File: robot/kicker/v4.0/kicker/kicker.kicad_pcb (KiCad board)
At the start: 6 copper layers, 172.6 x 120 mm, 181 parts, among them J1 BM08B-GHS-TBT, J10 SM08B-GHS-TB, J2 BM04B-PASS-1-TFT, J3 XT30-F, J4 Conn_ARM_JTAG_SWD_10, J5 2165711002, J6 2165711002, J7 SM12B-ZESS-TB, J8 SM08B-GHS-TB, J9 SM08B-GHS-TB, Q1 BSS138K, Q2 BSS138K, Q3 IXGA48N60A3, Q4 IXGA48N60A3, Q5 BSC0402NSATMA1, SW1 BTN0, SW2 SW_DIP_x04, SW3 RST, U1 TLV70030_SOT353, U2 TPS7B86, U3 STM32G474VETx, U4 SK9822, U5 AT25DF041x-UxN-x, U6 SK9822, U7 IX4427, U8 LT3757EMSE, Y1 Q13FC13500005, Y2 TAXM8M4RDBCCT2T

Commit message: Set preferred bank capacitor PN
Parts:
- C25, C26: value 1500uF 200V -> ESMQ201VSN152MR35S
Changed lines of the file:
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@@
 			)
 		)
-		(property "Value" "1500uF 200V"
+		(property "Value" "ESMQ201VSN152MR35S"
 			(at 5 -16.25 90)
 			(layer "B.Fab")
@@
 			)
 		)
+		(property "Value2" "1500uF 200V"
+			(at 0 0 -90)
+			(unlocked yes)
+			(layer "B.Fab")
+			(hide yes)
+			(effects
+				(font
+					(size 1 1)
+					(thickness 0.15)
+				)
+				(justify mirror)
+			)
+		)
 		(property ki_fp_filters "CP_*")
 		(sheetname "hv_kicker")
@@
 			)
 		)
-		(property "Value" "1500uF 200V"
+		(property "Value" "ESMQ201VSN152MR35S"
 			(at 5 -16.25 90)
 			(layer "B.Fab")
@@
 					(thickness 0.15)
 				)
+				(justify mirror)
+			)
+		)
+		(property "Value2" "1500uF 200V"
+			(at 0 0 -90)
+			(unlocked yes)
+			(layer "B.Fab")
+			(hide yes)
+			(effects
+				(font
+					(size 1 1)
+					(thickness 0.15)
+				)

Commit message: Update potentiometer values
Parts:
- RV1: value ACFG1 -> 3269P-1-103GLF
- RV2: value ACFG2 -> 3269P-1-103GLF
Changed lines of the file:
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@@
 		(tags "resistor")
 		(property "Reference" "R11"
-			(at -2.5 0 360)
+			(at -2.5 0 0)
 			(layer "F.SilkS")
 			(effects
@@
 		)
 		(property "Value" "10k"
-			(at 0 1.17 360)
+			(at 0 1.17 0)
 			(layer "F.Fab")
 			(effects
@@
 		)
 		(fp_text user "${REFERENCE}"
-			(at 0 0 360)
+			(at 0 0 0)
 			(layer "F.Fab")
 			(effects
@@
 		(tags "resistor")
 		(property "Reference" "R22"
-			(at 0 -1.25 360)
+			(at 0 -1.25 0)
 			(layer "F.SilkS")
 			(effects
@@
 		)
 		(property "Value" "10k"
-			(at 0 1.17 360)
+			(at 0 1.17 0)
 			(layer "F.Fab")
 			(effects
@@
 		)
 		(fp_text user "${REFERENCE}"
-			(at 0 0 360)
+			(at 0 0 0)
 			(layer "F.Fab")
 			(effects
@@
 		(tags "resistor")
 		(property "Reference" "R50"
-			(at 0 -1.65 360)
+			(at 0 -1.65 0)
 			(layer "F.SilkS")
 			(effects
@@
 		)
 		(property "Value" "1.47M"
-			(at 0 1.65 360)
+			(at 0 1.65 0)
 			(layer "F.Fab")
 			(effects
@@
 		)
 		(fp_text user "${REFERENCE}"
-			(at 0 0 360)
+			(at 0 0 0)
 			(layer "F.Fab")
 			(effects
@@
 		(tags "capacitor")
 		(property "Reference" "C5"
-			(at 0 1.25 360)
+			(at 0 1.25 0)
 			(layer "F.SilkS")
 			(effects
@@
 		)
 		(property "Value" "10u 50V"
-			(at 0 1.16 360)
+			(at 0 1.16 0)
 			(layer "F.Fab")
 			(effects
@@
 		)
 		(fp_text user "${REFERENCE}"
-			(at 0 0 360)
+			(at 0 0 0)
 			(layer "F.Fab")
 			(effects
@@
 			)
 		)
-		(property "Value" "ACFG1"
+		(property "Value" "3269P-1-103GLF"
 			(at 0 4.425001 135)
 			(layer "F.Fab")
@@
 			)
 		)
+		(property "Value2" "10k"
+			(at 0 0 135)
+			(unlocked yes)
+			(layer "F.Fab")
+			(hide yes)
+			(effects
+				(font
+					(size 1 1)
+					(thickness 0.15)
+				)
+			)
+		)
 		(property ki_fp_filters "Potentiometer*")
 		(sheetname "digital")
@@
 		(at 248 173 90)
 		(property "Reference" "SW2"
-			(at -4.75 0 360)
+			(at -4.75 0 0)
 			(layer "F.SilkS")
 			(effects
@@
 		(tags "resistor")
 		(property "Reference" "R10"
-			(at 0 1.5 360)
+			(at 0 1.5 0)
 			(layer "F.SilkS")
 			(effects
@@
 		)
 		(property "Value" "10k"
-			(at 0 1.17 360)
+			(at 0 1.17 0)
 			(layer "F.Fab")
 			(effects
@@
 		)
 		(fp_text user "${REFERENCE}"
-			(at 0 0 360)
+			(at 0 0 0)
 			(layer "F.Fab")
 			(effects
@@
 		(tags "resistor")
 		(property "Reference" "R20"
-			(at 2.5 0.25 360)
+			(at 2.5 0.25 0)
 			(layer "F.SilkS")
 			(effects
@@
 		)
 		(property "Value" "330"
-			(at 0 1.17 360)
+			(at 0 1.17 0)
 			(layer "F.Fab")
 			(effects
@@
 		)
 		(fp_text user "${REFERENCE}"
-			(at 0 0 360)
+			(at 0 0 0)
 			(layer "F.Fab")
 			(effects
@@
 		(tags "capacitor")
 		(property "Reference" "C6"
-			(at -2.5 0.25 360)
+			(at -2.5 0.25 0)
 			(layer "F.SilkS")
 			(effects
@@
 		)
 		(property "Value" "100n 50V"
-			(at 0 1.16 360)
+			(at 0 1.16 0)
 			(layer "F.Fab")
 			(effects
@@
 		)
 		(fp_text user "${REFERENCE}"
-			(at 0 0 360)
+			(at 0 0 0)
 			(layer "F.Fab")
 			(effects
@@
 		(tags "resistor")
 		(property "Reference" "R44"
-			(at -2.5 -0.25 360)
+			(at -2.5 -0.25 0)
 			(layer "F.SilkS")
 			(effects
@@
 		)
 		(property "Value" "10k"
-			(at 0 1.17 360)
+			(at 0 1.17 0)
 			(layer "F.Fab")
 			(effects
@@
 		)
 		(fp_text user "${REFERENCE}"
-			(at 0 0 360)
+			(at 0 0 0)
 			(layer "F.Fab")
 			(effects
@@
 		(tags "Diode SMC (DO-214AB)")
 		(property "Reference" "D12"
-			(at 0 4.500001 360)
+			(at 0 4.500001 0)
 			(layer "F.SilkS")
 			(effects
@@
 		)
 		(property "Value" "MURS460"
-			(at 0 4.199999 360)
+			(at 0 4.199999 0)
 			(layer "F.Fab")
 			(effects
@@
 		)
 		(fp_text user "${REFERENCE}"
-			(at 0 -1.9 360)
+			(at 0 -1.9 0)
 			(layer "F.Fab")
 			(effects
@@
 		(tags "resistor")
 		(property "Reference" "R38"
-			(at -2.5 -0.5 360)
+			(at -2.5 -0.5 0)
 			(layer "F.SilkS")
 			(effects
@@
 		)
 		(property "Value" "23.2k"
-			(at 0 1.17 360)
+			(at 0 1.17 0)
 			(layer "F.Fab")
 			(effects
@@
 		)
 		(fp_text user "${REFERENCE}"
-			(at 0 0 360)
+			(at 0 0 0)
 			(layer "F.Fab")
 			(effects
@@
 		(tags "resistor")
 		(property "Reference" "R49"
-			(at 0 -1.65 360)
+			(at 0 -1.65 0)
 			(layer "F.SilkS")
 			(effects
@@
 		)
 		(property "Value" "1.47M"
-			(at 0 1.65 360)
+			(at 0 1.65 0)
 			(layer "F.Fab")
 			(effects
@@
 		)
 		(fp_text user "${REFERENCE}"
-			(at 0 0 360)
+			(at 0 0 0)
 			(layer "F.Fab")
 			(effects
@@
 		(tags "resistor")
 		(property "Reference" "R57"
-			(at 2.5 0 360)
+			(at 2.5 0 0)
 			(layer "F.SilkS")
 			(effects
@@
 		)
 		(property "Value" "10"
-			(at 0 1.17 360)
+			(at 0 1.17 0)
 			(layer "F.Fab")
 			(effects
@@
 		)
 		(fp_text user "${REFERENCE}"
-			(at 0 0 360)
+			(at 0 0 0)
 			(layer "F.Fab")
 			(effects
@@
 		(tags "resistor")
 		(property "Reference" "R31"
-			(at -2.5 0 360)
+			(at -2.5 0 0)
 			(layer "F.SilkS")
 			(effects
@@
 		)
 		(property "Value" "10k"
-			(at 0 1.17 360)
+			(at 0 1.17 0)
 			(layer "F.Fab")
 			(effects
@@
 		)
 		(fp_text user "${REFERENCE}"
-			(at 0 0 360)
+			(at 0 0 0)
 			(layer "F.Fab")
 			(effects
@@
 		(tags "resistor")
 		(property "Reference" "R1"
-			(at -0.2 -2.3 360)
+			(at -0.2 -2.3 0)
 			(layer "F.SilkS")
 			(effects
@@
 		)
 		(property "Value" "330"
-			(at 0 1.17 360)
+			(at 0 1.17 0)
 			(layer "F.Fab")
 			(effects
@@
 		)
 		(fp_text user "${REFERENCE}"
-			(at 0 0 360)
+			(at 0 0 0)
 			(layer "F.Fab")
 			(effects
@@
 			)
 		)
-		(property "Value" "ACFG2"
+		(property "Value" "3269P-1-103GLF"
 			(at 0 4.425001 135)
 			(layer "F.Fab")
@@
 			)
 		)
+		(property "Value2" "10k"
+			(at 0 0 135)
+			(unlocked yes)
+			(layer "F.Fab")
+			(hide yes)
+			(effects
+				(font
+					(size 1 1)
+					(thickness 0.15)
+				)
+			)
+		)
 		(property ki_fp_filters "Potentiometer*")
 		(sheetname "digital")
@@
 		(tags "resistor")
 		(property "Reference" "R35"
-			(at -2.5 0.25 360)
+			(at -2.5 0.25 0)
 			(layer "F.SilkS")
 			(effects
@@
 		)
 		(property "Value" "10k"
-			(at 0 1.17 360)
+			(at 0 1.17 0)
 			(layer "F.Fab")
 			(effects
@@
 		)
 		(fp_text user "${REFERENCE}"
-			(at 0 0 360)
+			(at 0 0 0)
 			(layer "F.Fab")
 			(effects
@@
 		(at 180 144)
 		(property "Reference" "F3"
-			(at 0 4.500001 360)
+			(at 0 4.500001 0)
 			(layer "B.SilkS")
 			(effects
@@
 		)
 		(property "Value" "10A"
-			(at 0 -4.500001 360)
+			(at 0 -4.500001 0)
 			(layer "B.Fab")
 			(effects
@@
 		)
 		(property "Footprint" "AT-Fuses:3557-2"
-			(at 0 0 360)
+			(at 0 0 0)
 			(layer "B.Fab")
 			(hide yes)
@@
 		)
 		(property "Datasheet" ""
-			(at 0 0 360)
+			(at 0 0 0)
 			(layer "B.Fab")
 			(hide yes)
@@
 		)
 		(property "Description" "Fuse"
-			(at 0 0 360)
+			(at 0 0 0)
 			(layer "B.Fab")
 			(hide yes)
@@
 		)
 		(fp_text user "${REFERENCE}"
-			(at 0 0 360)
+			(at 0 0 0)
 			(layer "B.Fab")
 			(effects
@@
 		)
 		(property "Footprint" "AT-Connectors:2165711002"
-			(at 0 0 360)
+			(at 0 0 0)
 			(layer "B.Fab")
 			(hide yes)
@@
 		)
 		(property "Datasheet" ""
-			(at 0 0 360)
+			(at 0 0 0)
 			(layer "B.Fab")
 			(hide yes)
@@
 		)
 		(property "Description" "Generic connector, single row, 01x02, script generated (kicad-library-utils/schlib/autogen/connector/)"
-			(at 0 0 360)
+			(at 0 0 0)
 			(layer "B.Fab")
 			(hide yes)
@@
 		)
 		(property "Footprint" "AT-Connectors:2165711002"
-			(at 0 0 360)
+			(at 0 0 0)
 			(layer "B.Fab")
 			(hide yes)
@@
 		)
 		(property "Datasheet" ""
-			(at 0 0 360)
+			(at 0 0 0)
 			(layer "B.Fab")
 			(hide yes)
@@
 		)
 		(property "Description" "Generic connector, single row, 01x02, script generated (kicad-library-utils/schlib/autogen/connector/)"
-			(at 0 0 360)
+			(at 0 0 0)
 			(layer "B.Fab")
 			(hide yes)

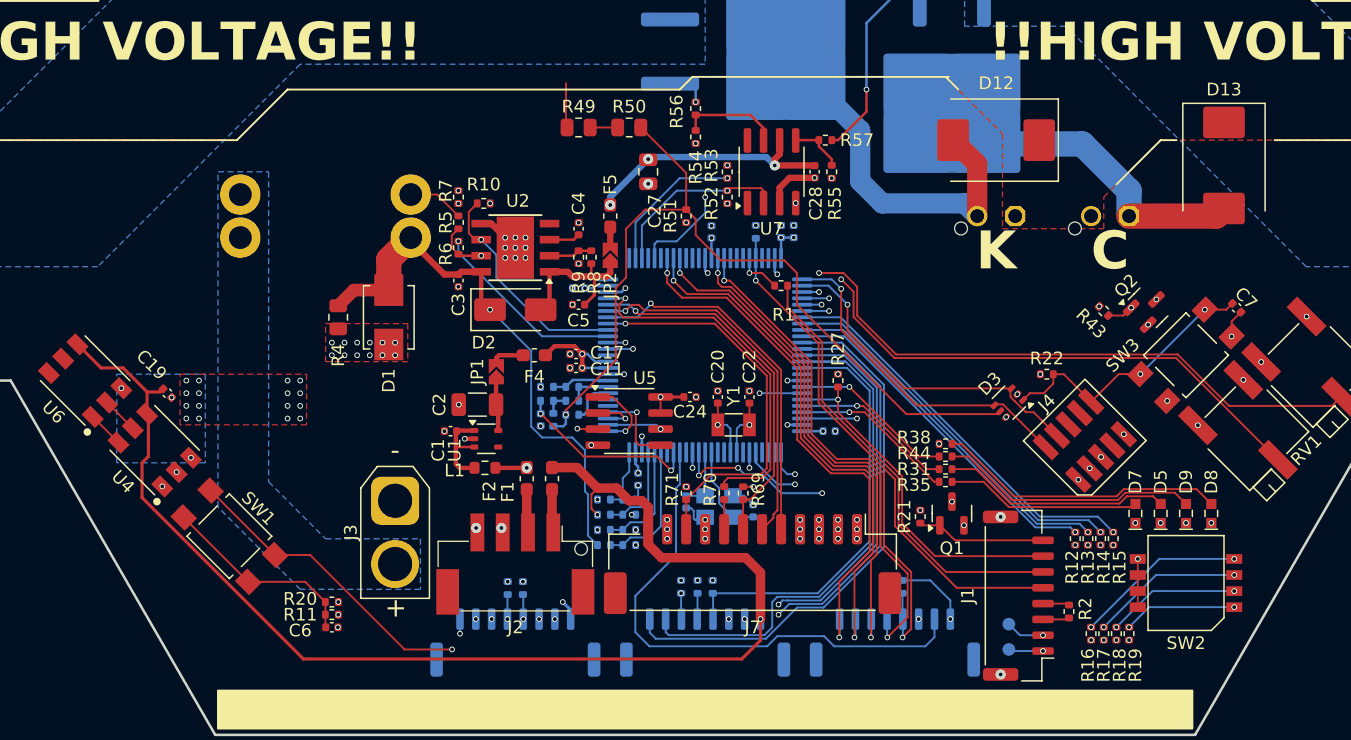
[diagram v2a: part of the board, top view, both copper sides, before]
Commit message: Update silkscreen & current sense resistor values
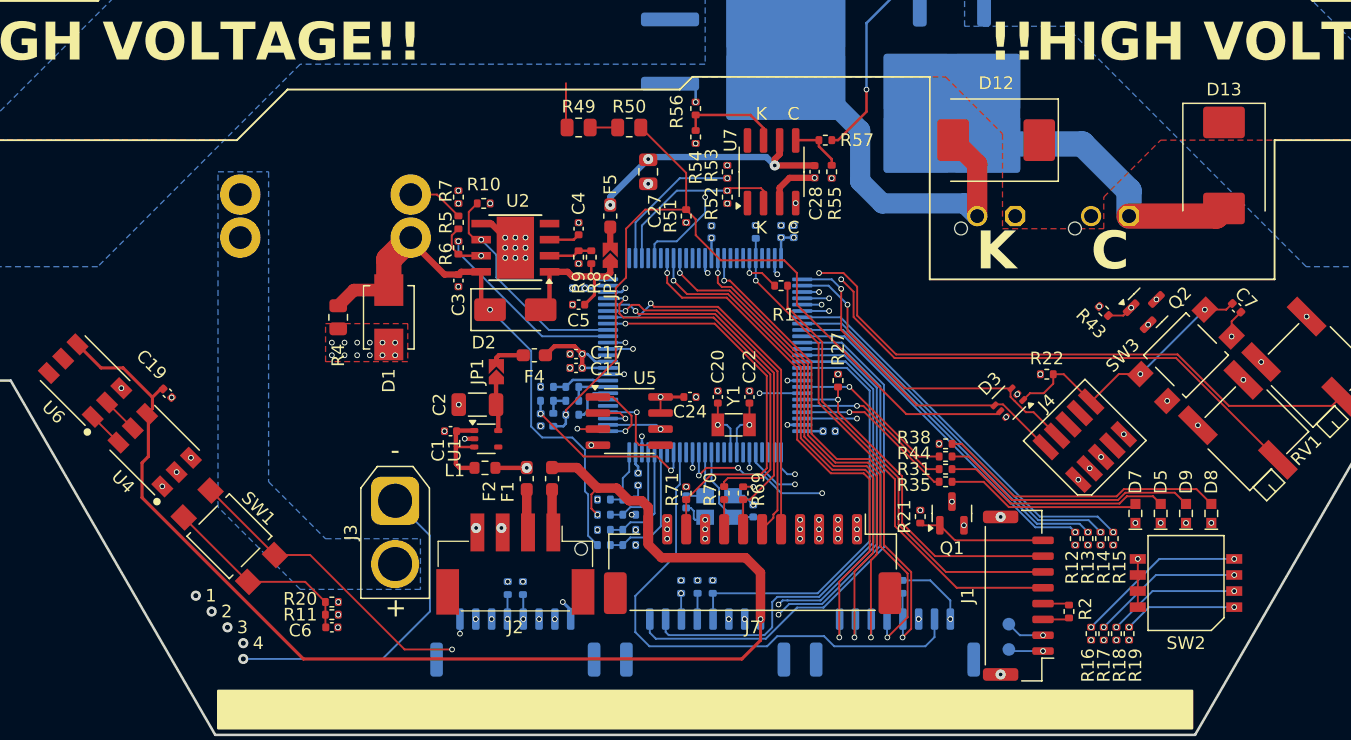
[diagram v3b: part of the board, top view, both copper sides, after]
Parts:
- R64, R65: value 4m -> PE1206FRM470R008L
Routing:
- net GND: track 84.9 -> 126.7 mm, vias 213 -> 202
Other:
- board text added: "1"
- board text added: "2"
- board text added: "3"
- board text added: "4"

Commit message: layout after connector fix done
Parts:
- removed J10: SM08B-GHS-TB, Connector_JST:JST_GH_SM08B-GHS-TB_1x08-1MP_P1.25mm_Horizontal
- added J11: JST-SM10B-GHS, Connector_JST:JST_GH_SM10B-GHS-TB_1x10-1MP_P1.25mm_Horizontal, F.Cu at (234.7, 172.6)
- added R79: 330, Resistor_SMD:R_0402_1005Metric, F.Cu at (207.5, 165.9)
- added R80: 100k, Resistor_SMD:R_0402_1005Metric, B.Cu at (214.9, 171.7)
- added R81: 100k, Resistor_SMD:R_0402_1005Metric, B.Cu at (216.0, 171.7)
- added R82: 100k, Resistor_SMD:R_0402_1005Metric, B.Cu at (234.4, 178.3)
- added R83: 100k, Resistor_SMD:R_0402_1005Metric, B.Cu at (234.4, 172.0)
- added R84: 100k, Resistor_SMD:R_0402_1005Metric, B.Cu at (234.4, 173.2)
- added R85: 330, Resistor_SMD:R_0402_1005Metric, F.Cu at (204.4, 177.9)
- added R86: 100k, Resistor_SMD:R_0402_1005Metric, F.Cu at (209.4, 177.9)
- added R87: 100k, Resistor_SMD:R_0402_1005Metric, F.Cu at (210.7, 177.9)
- J1: value BM08B-GHS-TBT -> JST-SM10B-GHS; footprint Connector_JST:JST_GH_BM08B-GHS-TBT_1x08-1MP_P1.25mm_Vertical -> Connector_JST:JST_GH_SM10B-GHS-TB_1x10-1MP_P1.25mm_Horizontal; moved to B.Cu
- R2, R69, R71: moved to B.Cu
- R76, R77, R78: moved to F.Cu
- moved J1 25.0 mm to (210.0, 177.7), turned to 180 degrees
- moved TP1 11.7 mm to (234.1, 166.6), turned to -135 degrees
- moved TP2 7.65 mm to (234.1, 168.6), turned to -135 degrees
- moved R77 5.90 mm to (206.9, 177.9), turned to 90 degrees
- moved R76 5.24 mm to (205.6, 177.9), turned to 90 degrees
- moved R71 5.17 mm to (211.5, 170.1), turned to 90 degrees
- moved R69 5.17 mm to (210.0, 170.1), turned to 90 degrees
- moved R78 4.75 mm to (208.2, 177.9)
- moved R2 4.69 mm to (234.4, 177.0), turned to 180 degrees
- moved J4 2.30 mm to (241.5, 160.0)
- moved D3 2.12 mm to (235.5, 157.2)
- moved R22 2.12 mm to (238.5, 155.0)
- moved R70 1.50 mm to (213.0, 165.9)
- moved J8 1.03 mm to (226.0, 177.7)
- moved R72 1.03 mm to (226.6, 173.3)
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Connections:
- J1 pad 1: /5v0_UPSTREAM -> +5V
- J1 pad 2: /3v3_UPSTREAM -> +3V3
- J1 pad 3: /GND_UPSTREAM -> GND
- J1 pad 4: /COMS.~{DET} -> GND
- J1 pad 5: /COMS.RX -> /Ball Sense/SENSE_BOOT_UART.BOOT0
- J1 pad 6: Net-(J1-Pin_6) -> /Ball Sense/SENSE_BOOT_UART.RST
- J1 pad 7: /COMS.BOOT0 -> Net-(J1-Pin_7)
- J1 pad 8: /COMS.RST -> /Ball Sense/SENSE_BOOT_UART.RX
- J7 pad 10: /Dribbler/DRIB_BOOT_UART.~{DET} -> Net-(J7-Pin_10)
- J7 pad 11: +3V3 -> GND
- J7 pad 12: +5V -> +3V3
- J7 pad 7: /Dribbler/DRIB_BOOT_UART.RX -> Net-(J7-Pin_7)
- J7 pad 8: Net-(J7-Pin_8) -> /Dribbler/DRIB_BOOT_UART.RX
- J7 pad 9: GND -> /Dribbler/DRIB_BOOT_UART.CTS
- R1 pad 1: Net-(J1-Pin_6) -> Net-(J11-Pin_8)
- R2 pad 1: /GND_UPSTREAM -> Net-(J11-Pin_9)
- R2 pad 2: /COMS.~{DET} -> /COMS.RTS
- R69 pad 2: /Dribbler/DRIB_BOOT_UART.RX -> /Dribbler/DRIB_BOOT_UART.CTS
- R70 pad 2: Net-(J7-Pin_8) -> Net-(J7-Pin_7)
- R71 pad 2: /Dribbler/DRIB_BOOT_UART.~{DET} -> /Dribbler/DRIB_BOOT_UART.RX
- R76 pad 2: /Ball Sense/SENSE_BOOT_UART.RX -> /Ball Sense/SENSE_BOOT_UART.CTS
- R77 pad 2: /Ball Sense/SENSE_BOOT_UART.~{DET} -> /Ball Sense/SENSE_BOOT_UART.RX
- R78 pad 1: Net-(J10-Pin_5) -> /Ball Sense/SENSE_BOOT_UART.TX
- R78 pad 2: /Ball Sense/SENSE_BOOT_UART.TX -> Net-(J1-Pin_7)
- U3 pad 3: unconnected-(U3-PE4-Pad3) -> /digital/DIP3
- U3 pad 43: /Dribbler/DRIB_BOOT_UART.~{DET} -> unconnected-(U3-PE12-Pad43)
- U3 pad 52: /digital/CMD_{CHIP} -> /Dribbler/DRIB_BOOT_UART.CTS
- U3 pad 53: /digital/CMD_{KICK} -> /Dribbler/DRIB_BOOT_UART.RTS
- U3 pad 54: unconnected-(U3-PB15-Pad54) -> /digital/CMD_{CHG}
- U3 pad 55: /digital/CMD_{CHG} -> /digital/CMD_{CHIP}
- U3 pad 56: unconnected-(U3-PD9-Pad56) -> /digital/CMD_{KICK}
- U3 pad 72: unconnected-(U3-PA11-Pad72) -> /COMS.CTS
- U3 pad 73: unconnected-(U3-PA12-Pad73) -> /COMS.RTS
- U3 pad 85: /digital/DIP3 -> /Ball Sense/SENSE_BOOT_UART.CTS
- U3 pad 86: /Ball Sense/SENSE_BOOT_UART.RST -> /Ball Sense/SENSE_BOOT_UART.RTS
- U3 pad 90: /Ball Sense/SENSE_BOOT_UART.~{DET} -> /Ball Sense/SENSE_BOOT_UART.RST
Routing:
- net /Ball Sense/SENSE_BOOT_UART.CTS: track 0.00 -> 51.7 mm, vias 0 -> 1
- net /Ball Sense/SENSE_BOOT_UART.RTS: track 0.00 -> 44.7 mm, vias 0 -> 1
- net /COMS.CTS: track 0.00 -> 44.3 mm, vias 0 -> 2
- net Net-(J11-Pin_8): track 0.00 -> 40.5 mm
- net /COMS.RTS: track 0.00 -> 38.1 mm, vias 0 -> 2
- net Net-(J1-Pin_6): track 35.5 -> 0.00 mm
- net /Ball Sense/SENSE_BOOT_UART.~{DET}: track 34.1 -> 0.00 mm
- net /Dribbler/DRIB_BOOT_UART.~{DET}: track 31.3 -> 0.00 mm, vias 1 -> 0
- net /Dribbler/DRIB_BOOT_UART.CTS: track 0.00 -> 24.9 mm, vias 0 -> 2
- net /Dribbler/DRIB_BOOT_UART.RTS: track 0.00 -> 21.6 mm, vias 0 -> 1
- net /COMS.RST: track 10.3 -> 17.6 mm, vias 0 -> 1
- net /Ball Sense/SENSE_BOOT_UART.RST: track 43.4 -> 36.5 mm, vias 0 -> 1
- net /Breakbeam/BB_RIGHT.AGPIO: track 42.2 -> 47.8 mm
- net /Ball Sense/SENSE_BOOT_UART.BOOT0: track 44.5 -> 40.3 mm, vias 0 -> 1
- net /Ball Sense/SENSE_BOOT_UART.RX: track 39.2 -> 42.9 mm, vias 2 -> 1
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
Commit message: add prod files
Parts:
- C5: footprint Capacitor_SMD:C_0402_1005Metric -> Capacitor_SMD:C_0805_2012Metric
- R36: value 8k -> 8.06k
- R41: value 650 -> 649
- R8: value 26.2k -> 26.1k
- moved C5 0.50 mm to (200.5, 151.0)
